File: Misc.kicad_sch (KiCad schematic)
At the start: 8 parts, among them J2 SWD, J3 RMF, SW1 SW_Push, SW2 RST

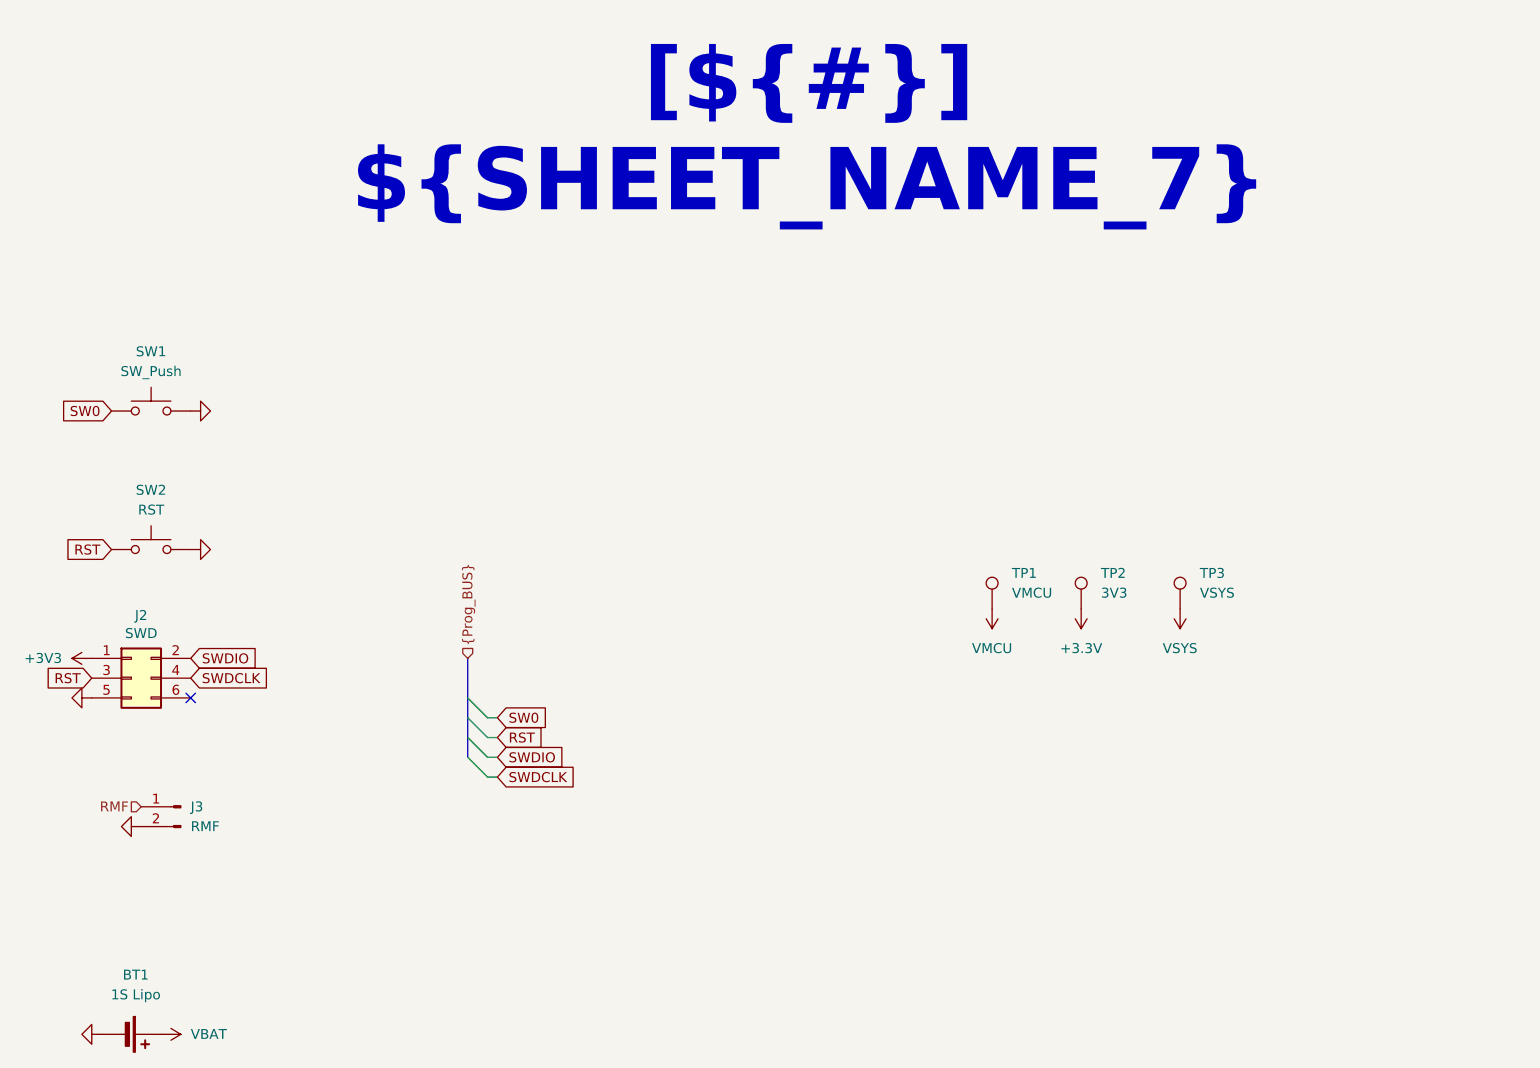
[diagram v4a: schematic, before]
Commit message: Minor schematic adjustments
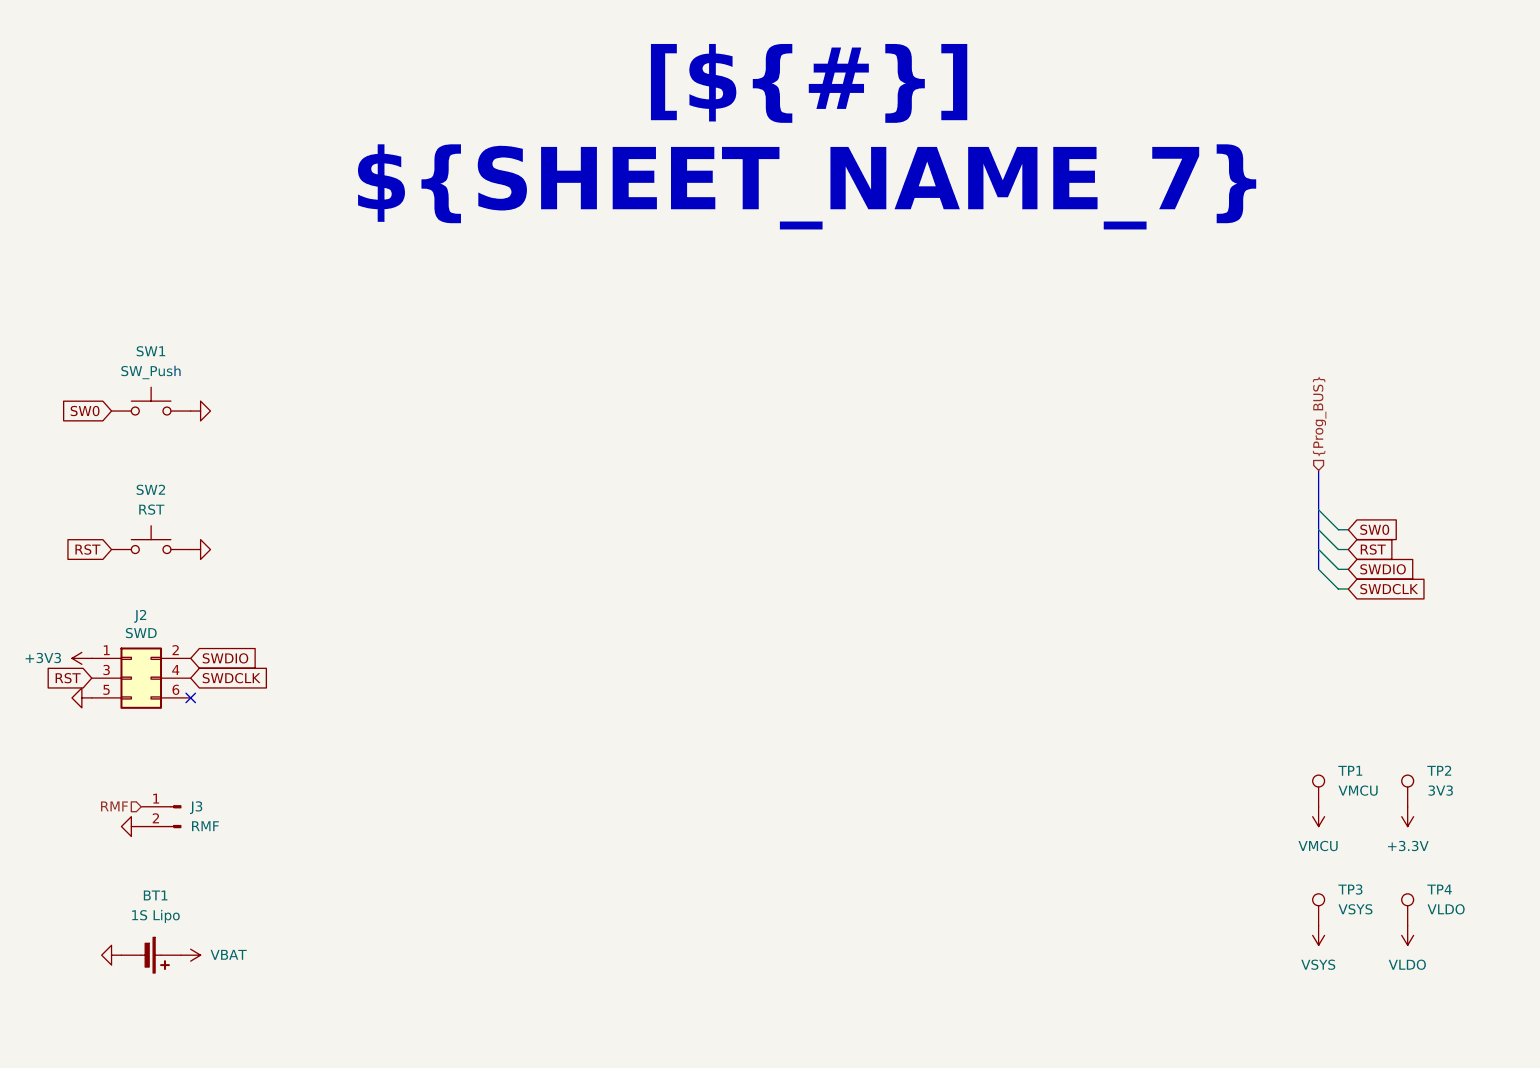
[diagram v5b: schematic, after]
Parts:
- added TP4: VLDO, TestPoint:TestPoint_Pad_D1.0mm, symbol Connector:TestPoint
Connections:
- new net VLDO: TP4.1
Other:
- moved on the sheet: BT1, TP1, TP2, TP3

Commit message: Minor tweaks
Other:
- moved on the sheet: TP1, TP2
